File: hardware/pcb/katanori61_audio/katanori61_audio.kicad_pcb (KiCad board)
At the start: 4 copper layers, 82 x 34 mm, 187 parts, among them J16 XU316 JTAG, J21 RISER PWR, J22 RISER SIG, J23 SPK, Q103 LBSS138WT1G, Q104 S9013W, U102 XU316-1024-QF60B-C32, U103 W25Q32JVSSIQ, U104 MSM261DHP006, U105 MSM261DHP006, U106 SN74LVC125APWR, U108 TLV320AIC3204IRHBR, U109 TPA6211A1DGNR, U110 TPS62827DMQR, U111 ME6211C18M5G-N, U112 TPS62065DSGR, U118 SGM2036S-3.3XXDH4G/TR, U5 ESP32-S3-WROOM-1U-N16R8, X101 24MHz 12pF

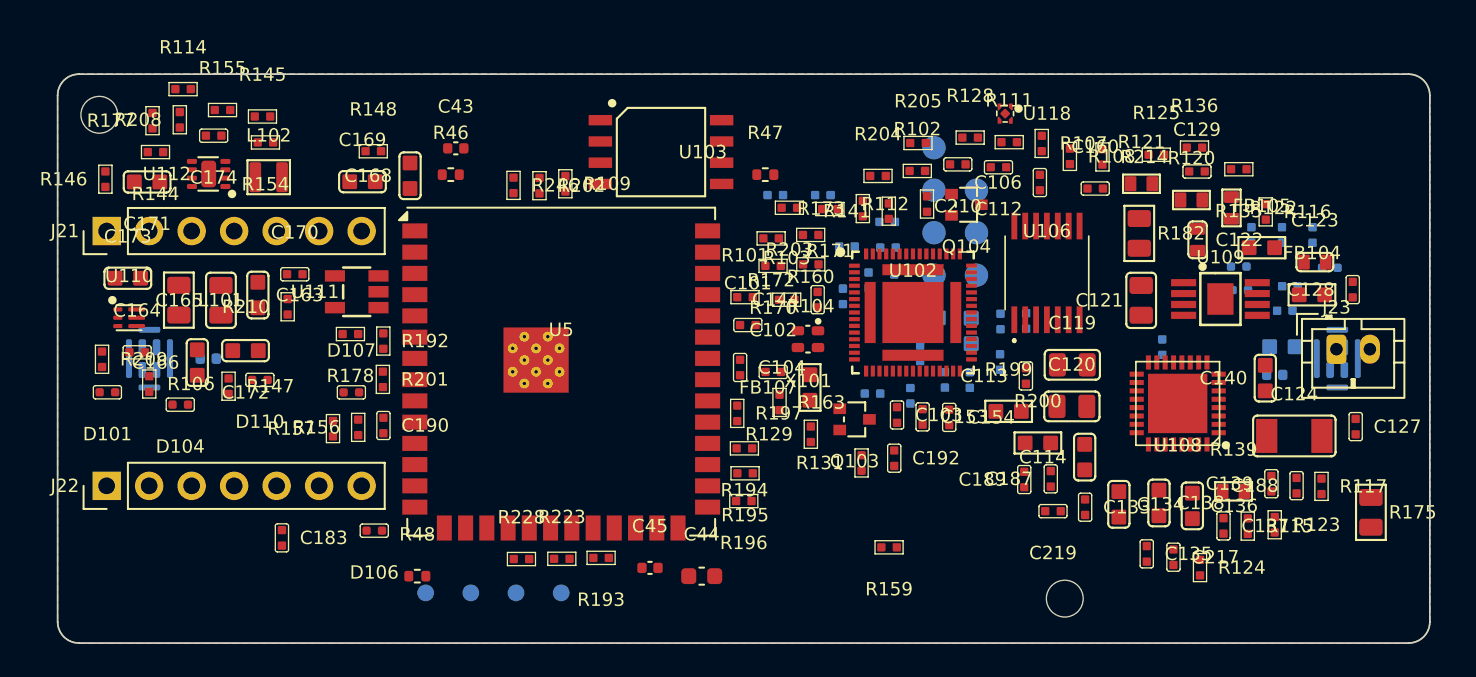
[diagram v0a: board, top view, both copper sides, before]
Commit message: 音声の板: 配置と配線（別スレッド katanori-83）。DRC エラー 0・未接続 0
- 別スレッドの作業（gen_pcb_audio.py --route --keep で再現）。XU316 の周り（Flash・JTAG・RST_N・SCL・LDO_SELECT）は手で引いた
- こちら（katanori-a7）で確かめた: KiCad の DRC（ゾーン再充填）エラー 0・未接続 0、check_sch_voice.py 0 件、
  板のパッドのネットと回路図のネットリストが全ピンで 1 対 1（名前の "/" 以外の違い無し）
- 残る警告: via_dangling 10・hole_to_hole 2・J16 の「未実装」属性が回路図と違う・シルク
- ⚠ 音の面（電源とマイク・コーデックの距離・GNDA・水晶・内層 2 の GND を外したこと）は、まだ誰も見ていない
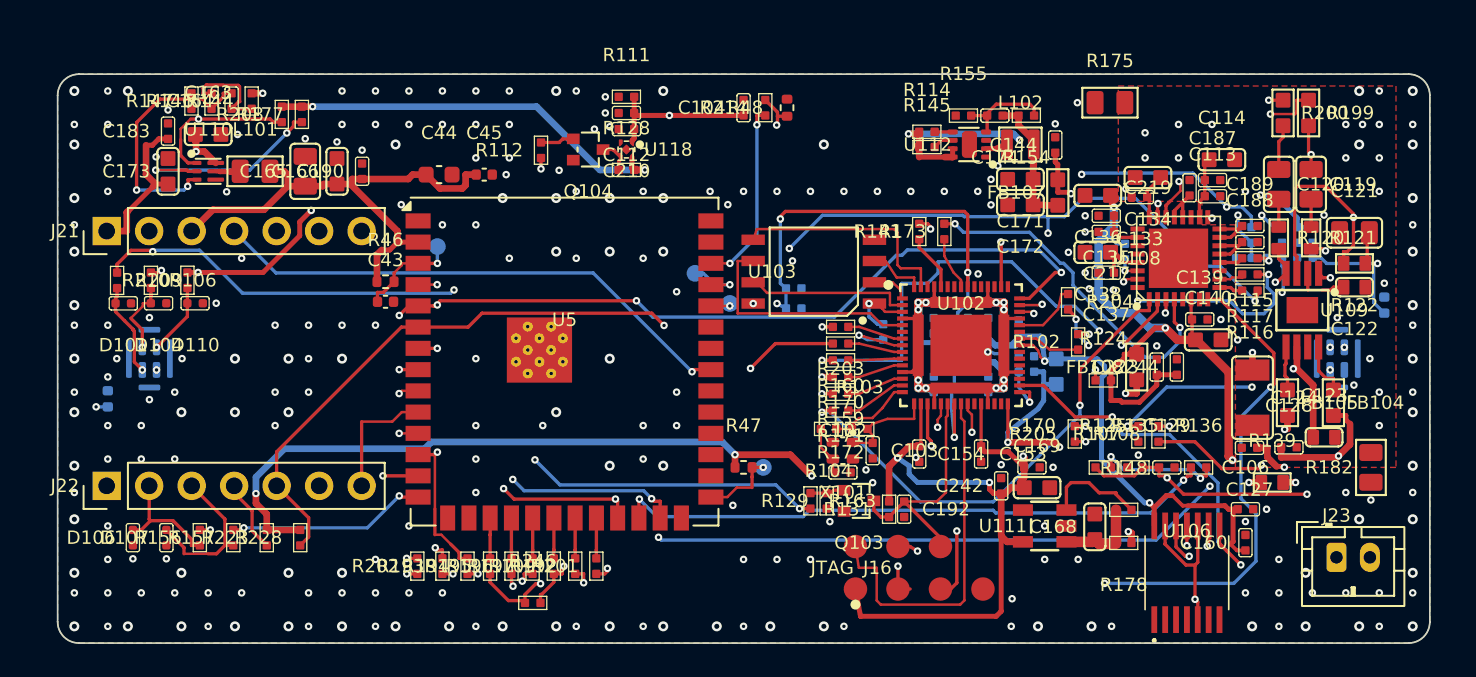
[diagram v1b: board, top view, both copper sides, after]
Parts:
- removed ? (x2): , MountingHole:MountingHole_2.2mm_M2
- removed the C105 at (106.0, 56.3)
- removed the C112 at (96.2, 45.6)
- removed the C122 at (108.1, 49.9)
- removed the R105 at (111.4, 49.6)
- removed the R178 at (57.5, 55.5)
- removed the R205 at (91.4, 44.1)
- removed the R209 at (42.7, 57.0)
- removed the R214 at (102.5, 45.0)
- removed the R48 at (61.5, 70.0)
- removed the U103 at (76.1, 44.7)
- added C120: 22uF, voicepe:C0805, F.Cu at (113.0, 46.6)
- added C127: 10nF, voicepe:C0402, F.Cu at (111.2, 62.3)
- added C143: 100nF, voicepe:C0402, B.Cu at (95.6, 54.1)
- added C301: 100nF, Capacitor_SMD:C_0402_1005Metric, B.Cu at (43.0, 59.4)
- added C302: 100nF, Capacitor_SMD:C_0402_1005Metric, B.Cu at (119.3, 53.8)
- added D112: SLESDPSA0402V05, voicepe:ESD-0402, B.Cu at (114.6, 51.0)
- added R210: 100R, voicepe:R0402, F.Cu at (47.8, 52.3)
- added R47: 10K, Resistor_SMD:R_0402_1005Metric, F.Cu at (81.0, 63.5)
- added U106: SN74LVC125APWR, voicepe:SN74LVC125APWR, F.Cu at (107.5, 69.8)
- added U110: TPS62827DMQR, voicepe:DFN6-0.5-1.5X1.5X0.65MM, F.Cu at (49.0, 45.8)
- C101, R101, R123: moved to B.Cu
- C105: renamed from U110; value TPS62827DMQR -> 100nF; footprint voicepe:DFN6-0.5-1.5X1.5X0.65MM -> voicepe:C0402; moved to B.Cu
- C112: renamed from R47; value 10K -> 100nF; footprint Resistor_SMD:R_0402_1005Metric -> voicepe:C0402
- C122: renamed from U106; value SN74LVC125APWR -> 100nF; footprint voicepe:SN74LVC125APWR -> voicepe:C0603_v2
- C223, C242, C244, FB108, J16: moved to F.Cu
- R105: renamed from R130; value 100R -> 0R
- R130: renamed from R210; moved to B.Cu
- R178: renamed from C143; value 100nF -> 0R; footprint voicepe:C0402 -> voicepe:R0402; moved to F.Cu
- R205: renamed from C127; value 10nF -> 0R; footprint voicepe:C0402 -> voicepe:R0402
- R209: renamed from D112; value SLESDPSA0402V05 -> 0R; footprint voicepe:ESD-0402 -> voicepe:R0402; moved to F.Cu
- R214: renamed from C301; value 100nF -> 0R; footprint Capacitor_SMD:C_0402_1005Metric -> voicepe:R0402; moved to F.Cu
- R48: renamed from C302; value 100nF -> 10K; footprint Capacitor_SMD:C_0402_1005Metric -> Resistor_SMD:R_0402_1005Metric; moved to F.Cu
- U103: renamed from C120; value 22uF -> W25Q32JVSSIQ; footprint voicepe:C0805 -> voicepe:SOIC8-1.27-5.3X5.3MM
- moved R209 72.5 mm to (43.6, 52.3), turned to 270 degrees
- moved C105 70.0 mm to (114.1, 49.6), turned to 270 degrees
- moved R130 61.4 mm to (115.0, 49.6)
- moved C171 52.2 mm to (97.5, 46.3)
- moved R148 49.7 mm to (103.7, 66.0)
- moved C172 47.1 mm to (97.5, 47.8)
- moved C174 46.7 mm to (96.0, 42.5)
- moved C168 46.0 mm to (102.0, 67.1)
- moved C170 45.5 mm to (98.2, 63.5)
- moved R154 45.5 mm to (97.9, 42.5)
- moved U112 45.5 mm to (94.5, 44.2)
- moved L102 45.0 mm to (97.5, 44.2)
- moved R114 44.5 mm to (92.0, 43.4)
- moved R155 44.3 mm to (94.1, 42.5)
- moved C169 44.3 mm to (98.5, 64.7)
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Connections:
- C105 pad 1: 3V3_EN -> VDD_MIC
- C105 pad 2: 3V3_PG -> GND
- C112 pad 1: V33 -> VDD_MIC
- C112 pad 2: ESP_BOOT -> GND
- C122 pad 1: GND -> GNDA
- C122 pad 2: GND -> N_U109_BYPASS
- R105 pad 1: N_U105_VDD -> MIC_CLK_M
- R105 pad 2: VDD_MIC -> N_U105_CLK
- R130 pad 1: R_ -> N_U105_VDD
- R178 pad 1: VDD -> V33
- R178 pad 2: GND -> N_U111_IN
- R205 pad 1: SPKO -> N_U102_X0D36
- R205 pad 2: GNDA -> I2S2_MCLK
- R209 pad 1: GND -> MIC_CLK_M
- R209 pad 2: N_U105_VDD -> N_U104_CLK
- R214 pad 1: R_ -> MIC_MUTE
- R214 pad 2: GND -> MUTE_ON
- R48 pad 1: N_U105_VDD -> MUTE_ON
- U103 pad 1: N_C221_Pad1 -> QSPI_CS_N
- U103 pad 2: N_C120_Pad2 -> QSPI_D1
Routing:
- net V33: track 0.00 -> 165.0 mm, vias 0 -> 9
- net MIC_DATA_M: track 0.00 -> 113.1 mm, vias 0 -> 5
- net V5: track 0.00 -> 109.0 mm, vias 0 -> 6
- net MIC_CLK_M: track 0.00 -> 100.6 mm, vias 0 -> 5
- net I2S_DIN_SEC: track 0.00 -> 96.1 mm, vias 0 -> 4
- net VDD_MIC: track 0.00 -> 90.2 mm, vias 0 -> 4
- net SDA: track 0.00 -> 85.1 mm, vias 0 -> 6
- net SCL: track 0.00 -> 82.0 mm, vias 0 -> 5
- net MUTE_ON: track 0.00 -> 81.2 mm, vias 0 -> 3
- net I2S_BCLK: track 0.00 -> 78.9 mm, vias 0 -> 5
- net VDDIO: track 0.00 -> 75.2 mm, vias 0 -> 7
- net VDD: track 0.00 -> 63.7 mm, vias 0 -> 13
- net I2S_DIN_ESP: track 0.00 -> 61.7 mm, vias 0 -> 3
- net I2S_LRCK: track 0.00 -> 57.9 mm, vias 0 -> 4
- net I2S_MCLK: track 0.00 -> 55.8 mm, vias 0 -> 3
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- added copper zone on F.Cu, net GNDA
- added copper zone on In1.Cu, net GNDA
- removed copper zone on In2.Cu, net GND
